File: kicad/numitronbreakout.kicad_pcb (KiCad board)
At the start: 4 copper layers, 60 x 100 mm, 12 parts, among them J1 Conn_01x06, U1 HV5812WG-G, U2 LM317_TO-220, U3 LM317_TO-220, U4 IV-12, U5 IV-12

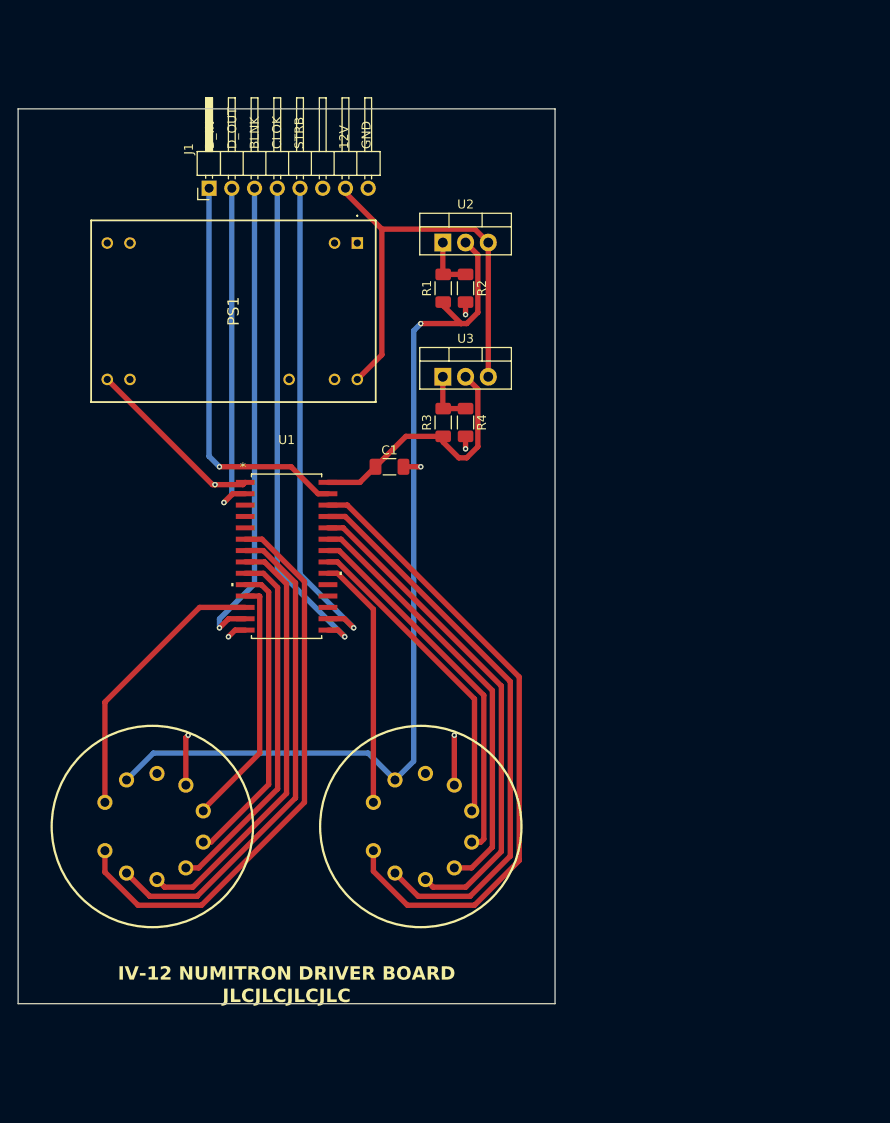
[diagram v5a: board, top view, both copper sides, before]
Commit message: updated pin connector, layout
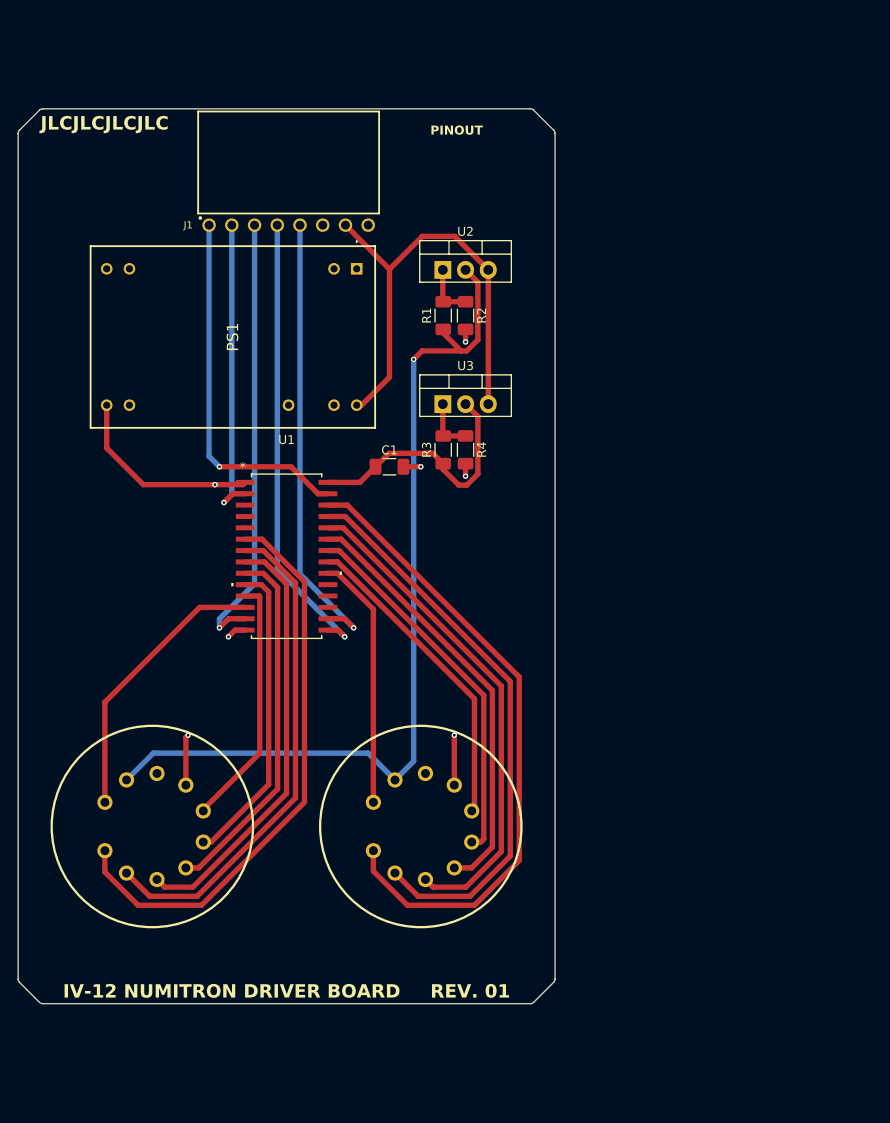
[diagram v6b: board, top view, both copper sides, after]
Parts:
- J1: footprint Connector_PinHeader_2.54mm:PinHeader_1x08_P2.54mm_Horizontal -> NewFootprints:66100811722
- moved J1 9.00 mm to (150.2, 60.3), turned to 180 degrees
- moved R1 3.06 mm to (167.5, 73.1)
- moved R2 3.06 mm to (170.0, 73.1)
- moved R3 3.06 mm to (167.5, 88.1)
- moved R4 3.06 mm to (170.0, 88.1)
- moved U2 3.06 mm to (167.5, 68.0)
- moved U3 3.06 mm to (167.5, 83.0)
- moved PS1 2.88 mm to (157.8, 67.9)
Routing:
- net STROBE: track 54.4 -> 50.8 mm
- net D_OUT: track 37.8 -> 34.1 mm
- net D_IN: track 44.5 -> 40.9 mm
- net CLOCK: track 54.9 -> 51.3 mm
- net BLANKING: track 53.5 -> 49.9 mm
- net +1V5: track 103.2 -> 100.0 mm
- net +12V: track 51.5 -> 53.4 mm
- net +30V: track 90.6 -> 92.3 mm
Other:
- outline, holes or cut-outs redrawn
- board text added: "PINOUT"
- board text added: "REV. 01"
- board text removed: "12V"
- board text removed: "BLNK"
- board text removed: "CLOK"
- board text removed: "D_IN"
- board text removed: "D_OUT"
- board text removed: "GND"
- board text removed: "STRB"
